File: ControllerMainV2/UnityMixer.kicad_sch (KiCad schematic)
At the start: 50 parts, among them IC17 TMUX6112PWR, IC18 TMUX6112PWR, IC19 TMUX6112PWR, U10 TL072, U18 TL074, U9 TL074

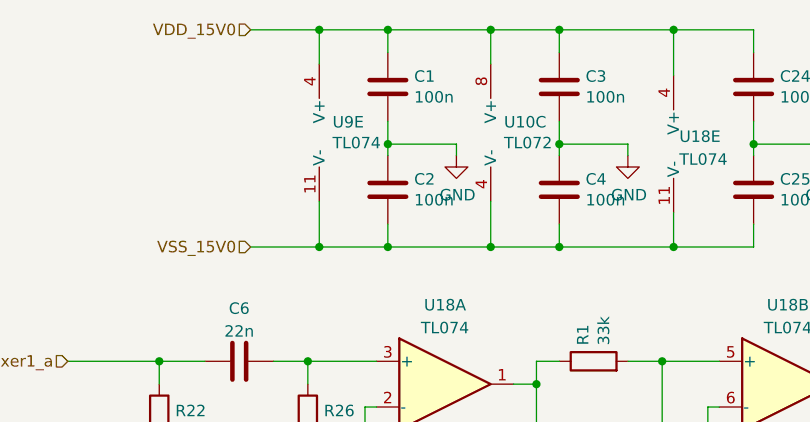
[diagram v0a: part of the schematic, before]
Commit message: Main mostly wired. Push for replacement
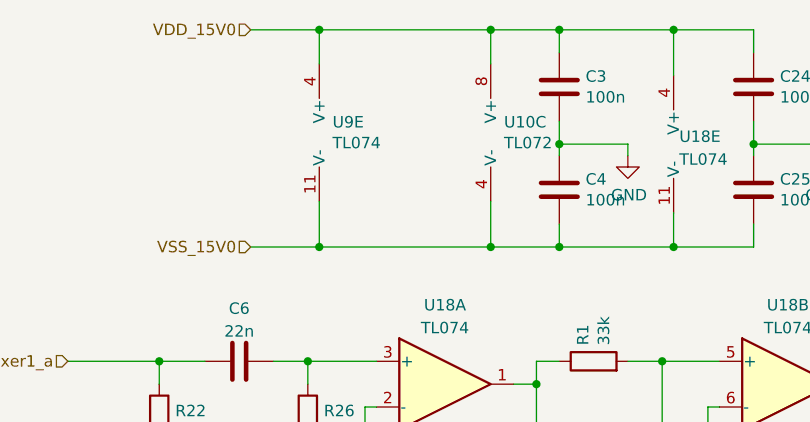
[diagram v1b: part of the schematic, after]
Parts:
- removed C1, C2: 100n, Capacitor_SMD:C_1206_3216Metric_Pad1.33x1.80mm_HandSolder, symbol Device:C
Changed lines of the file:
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@@
   (junction (at 238.125 212.725) (diameter 0) (color 0 0 0 0)
   )
-  (junction (at 100.965 43.815) (diameter 0) (color 0 0 0 0)
-  )
   (junction (at 73.025 220.345) (diameter 0) (color 0 0 0 0)
   )
-  (junction (at 100.965 19.685) (diameter 0) (color 0 0 0 0)
-  )
   (junction (at 131.445 191.135) (diameter 0) (color 0 0 0 0)
   )
@@
   (junction (at 120.015 19.685) (diameter 0) (color 0 0 0 0)
   )
-  (junction (at 100.965 32.385) (diameter 0) (color 0 0 0 0)
-  )
   (junction (at 258.445 78.105) (diameter 0) (color 0 0 0 0)
   )
@@
     (stroke (width 0) (type default) (color 0 0 0 0))
   )
-  (wire (pts (xy 100.965 32.385) (xy 108.585 32.385))
-    (stroke (width 0) (type default) (color 0 0 0 0))
-  )
   (wire (pts (xy 201.295 75.565) (xy 201.295 84.455))
     (stroke (width 0) (type default) (color 0 0 0 0))
@@
     (stroke (width 0) (type default) (color 0 0 0 0))
   )
-  (wire (pts (xy 100.965 43.815) (xy 112.395 43.815))
+  (wire (pts (xy 93.345 43.815) (xy 112.395 43.815))
     (stroke (width 0) (type default) (color 0 0 0 0))
   )
@@
     (stroke (width 0) (type default) (color 0 0 0 0))
   )
-  (wire (pts (xy 100.965 41.275) (xy 100.965 43.815))
-    (stroke (width 0) (type default) (color 0 0 0 0))
-  )
   (wire (pts (xy 255.905 78.105) (xy 258.445 78.105))
     (stroke (width 0) (type default) (color 0 0 0 0))
@@
     (stroke (width 0) (type default) (color 0 0 0 0))
   )
-  (wire (pts (xy 108.585 32.385) (xy 108.585 33.655))
-    (stroke (width 0) (type default) (color 0 0 0 0))
-  )
   (wire (pts (xy 201.295 59.055) (xy 201.295 71.755))
     (stroke (width 0) (type default) (color 0 0 0 0))
   )
-  (wire (pts (xy 100.965 22.225) (xy 100.965 19.685))
-    (stroke (width 0) (type default) (color 0 0 0 0))
-  )
   (wire (pts (xy 238.125 212.725) (xy 239.395 212.725))
     (stroke (width 0) (type default) (color 0 0 0 0))
@@
     (stroke (width 0) (type default) (color 0 0 0 0))
   )
-  (wire (pts (xy 100.965 32.385) (xy 100.965 29.845))
-    (stroke (width 0) (type default) (color 0 0 0 0))
-  )
   (wire (pts (xy 187.325 206.375) (xy 182.245 206.375))
     (stroke (width 0) (type default) (color 0 0 0 0))
   )
-  (wire (pts (xy 100.965 43.815) (xy 93.345 43.815))
-    (stroke (width 0) (type default) (color 0 0 0 0))
-  )
   (wire (pts (xy 128.905 220.345) (xy 133.985 220.345))
     (stroke (width 0) (type default) (color 0 0 0 0))
@@
     (stroke (width 0) (type default) (color 0 0 0 0))
   )
-  (wire (pts (xy 100.965 19.685) (xy 93.345 19.685))
-    (stroke (width 0) (type default) (color 0 0 0 0))
-  )
   (wire (pts (xy 89.535 191.135) (xy 89.535 193.675))
     (stroke (width 0) (type default) (color 0 0 0 0))
@@
     (stroke (width 0) (type default) (color 0 0 0 0))
   )
-  (wire (pts (xy 100.965 19.685) (xy 112.395 19.685))
+  (wire (pts (xy 93.345 19.685) (xy 112.395 19.685))
     (stroke (width 0) (type default) (color 0 0 0 0))
   )
@@
   )
   (wire (pts (xy 97.155 201.295) (xy 116.205 201.295))
-    (stroke (width 0) (type default) (color 0 0 0 0))
-  )
-  (wire (pts (xy 100.965 33.655) (xy 100.965 32.385))
     (stroke (width 0) (type default) (color 0 0 0 0))
   )
@@
       (effects (font (size 1.27 1.27)) hide)
     )
-    (pin "1")
-  )
-  (symbol (lib_id "Device:C") (at 100.965 26.035 0) (unit 1)
-    (in_bom yes) (on_board yes)
-    (property "Reference" "C1" (id 0) (at 103.886 24.8666 0)
-      (effects (font (size 1.27 1.27)) (justify left))
-    )
-    (property "Value" "100n" (id 1) (at 103.886 27.178 0)
-      (effects (font (size 1.27 1.27)) (justify left))
-    )
-    (property "Footprint" "Capacitor_SMD:C_1206_3216Metric_Pad1.33x1.80mm_HandSolder" (id 2) (at 101.9302 29.845 0)
-      (effects (font (size 1.27 1.27)) hide)
-    )
-    (property "Datasheet" "~" (id 3) (at 100.965 26.035 0)
-      (effects (font (size 1.27 1.27)) hide)
-    )
-    (pin "1")
-    (pin "2")
-  )
-  (symbol (lib_id "Device:C") (at 100.965 37.465 0) (unit 1)
-    (in_bom yes) (on_board yes)
-    (property "Reference" "C2" (id 0) (at 103.886 36.2966 0)
-      (effects (font (size 1.27 1.27)) (justify left))
-    )
-    (property "Value" "100n" (id 1) (at 103.886 38.608 0)
-      (effects (font (size 1.27 1.27)) (justify left))
-    )
-    (property "Footprint" "Capacitor_SMD:C_1206_3216Metric_Pad1.33x1.80mm_HandSolder" (id 2) (at 101.9302 41.275 0)
-      (effects (font (size 1.27 1.27)) hide)
-    )
-    (property "Datasheet" "~" (id 3) (at 100.965 37.465 0)
-      (effects (font (size 1.27 1.27)) hide)
-    )
-    (pin "1")
-    (pin "2")
-  )
-  (symbol (lib_id "power:GND") (at 108.585 33.655 0) (unit 1)
-    (in_bom yes) (on_board yes)
-    (property "Reference" "#PWR02" (id 0) (at 108.585 40.005 0)
-      (effects (font (size 1.27 1.27)) hide)
-    )
-    (property "Value" "GND" (id 1) (at 108.712 38.0492 0))
-    (property "Footprint" "" (id 2) (at 108.585 33.655 0)
-      (effects (font (size 1.27 1.27)) hide)
-    )
-    (property "Datasheet" "" (id 3) (at 108.585 33.655 0)
-      (effects (font (size 1.27 1.27)) hide)
-    )

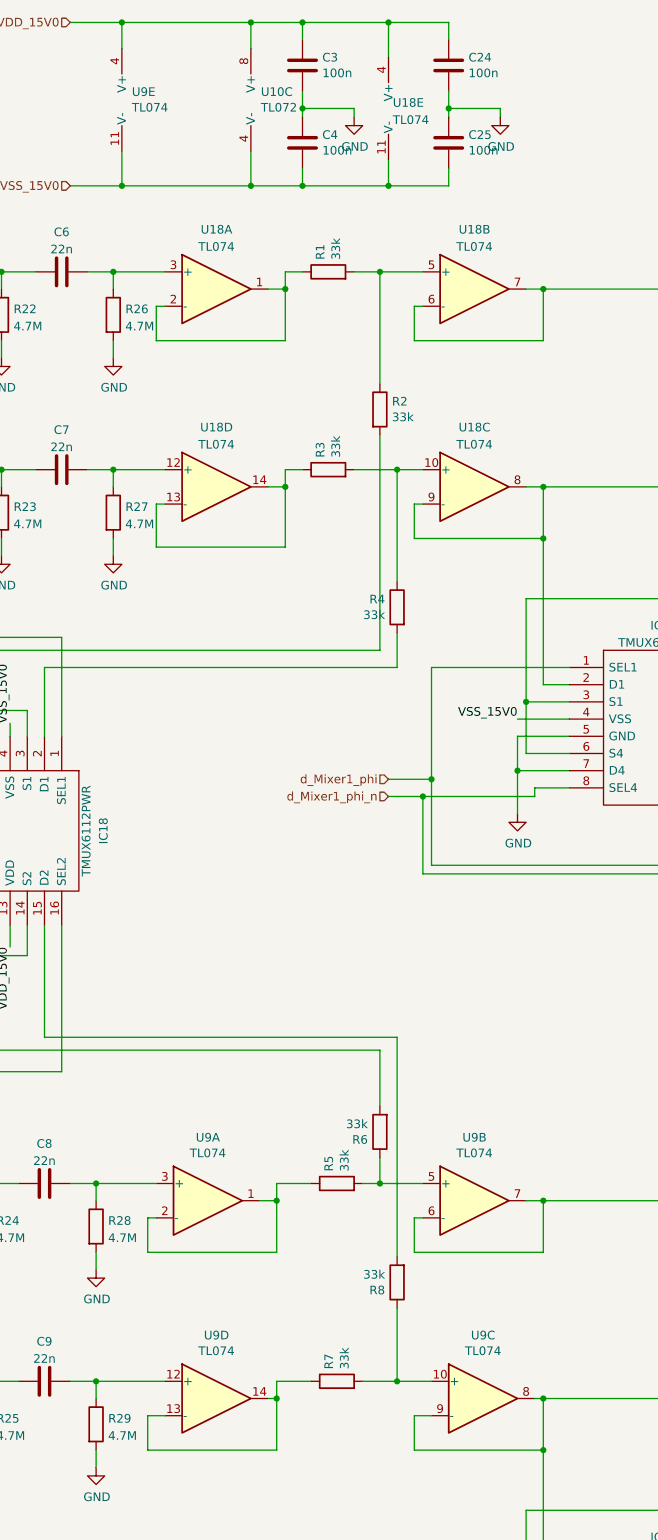
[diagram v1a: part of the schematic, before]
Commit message: Mixer, controll and supply wiring done. Matrix connections missing
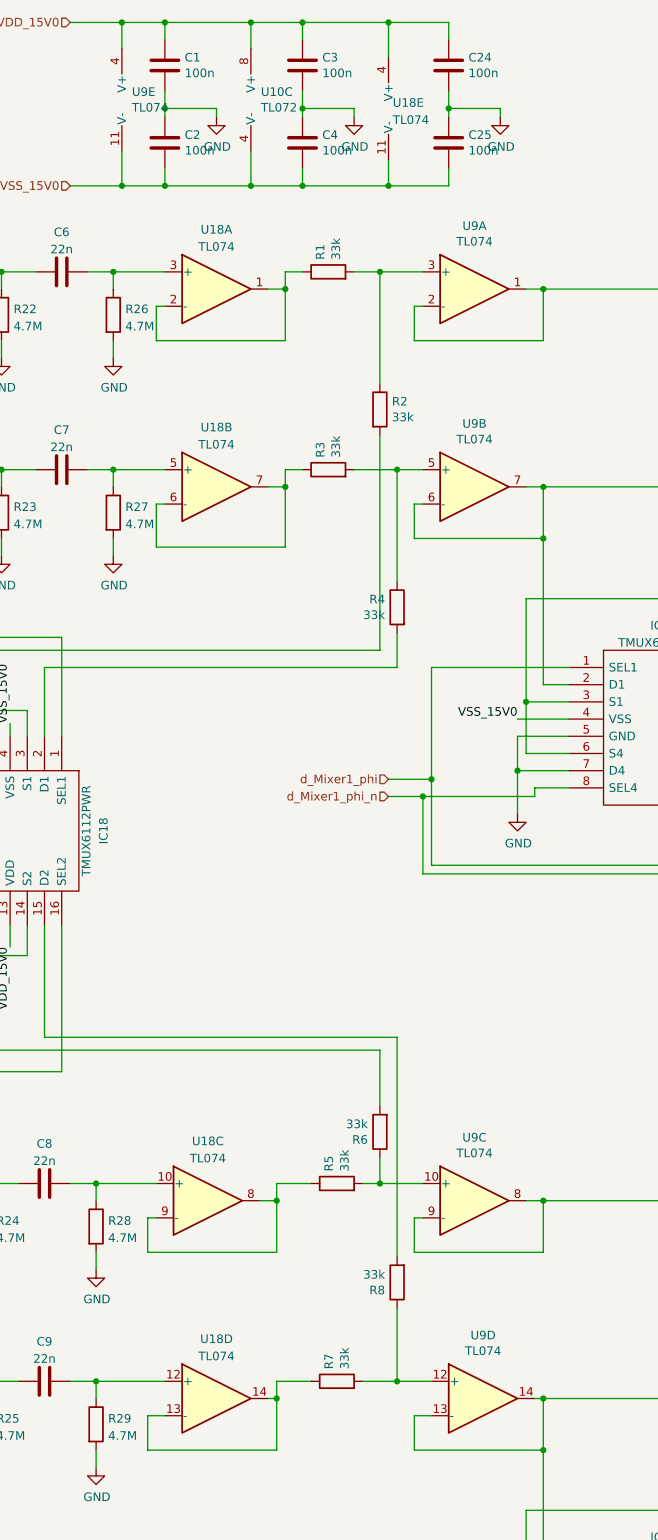
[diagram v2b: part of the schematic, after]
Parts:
- added C1, C2: 100n, Capacitor_SMD:C_1206_3216Metric_Pad1.33x1.80mm_HandSolder, symbol Device:C
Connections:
- net GND: now also C1.2, C2.1
- net VDD_15V0: now also C1.1
- net VSS_15V0: now also C2.2
- net at U9.1, U9.2 (-): now also R9.2; no longer R5.1
- net at C8.2, R28.1: now also U18.10 (+); no longer U9.3 (+)
- net at R5.2, R6.1: now also U9.10 (+); no longer U9.5 (+)
- net at U9.6 (-), U9.7: now also IC17.15 (D2), IC17.2 (D1); no longer R12.1
- net at U18.6 (-), U18.7: now also R3.1; no longer R9.2
- net at R1.2, R2.1: now also U9.3 (+); no longer U18.5 (+)
- net at U18.13 (-), U18.14: now also R7.1; no longer R3.1
- net at R3.2, R4.1: now also U9.5 (+); no longer U18.10 (+)
- net at U9.13 (-), U9.14: now also IC19.15 (D2), IC19.2 (D1); no longer R7.1
- net at R7.2, R8.1: now also U9.12 (+); no longer U9.10 (+)
- net at U9.8, U9.9 (-): now also R12.1; no longer IC19.15 (D2), IC19.2 (D1)
- net at C9.2, R29.1: now also U18.12 (+); no longer U9.12 (+)
- net at U18.8, U18.9 (-): now also R5.1; no longer IC17.15 (D2), IC17.2 (D1)
- net at C7.2, R27.1: now also U18.5 (+); no longer U18.12 (+)
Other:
- moved on the sheet: U18B, U18C, U18D, U9A, U9B, U9C, U9D

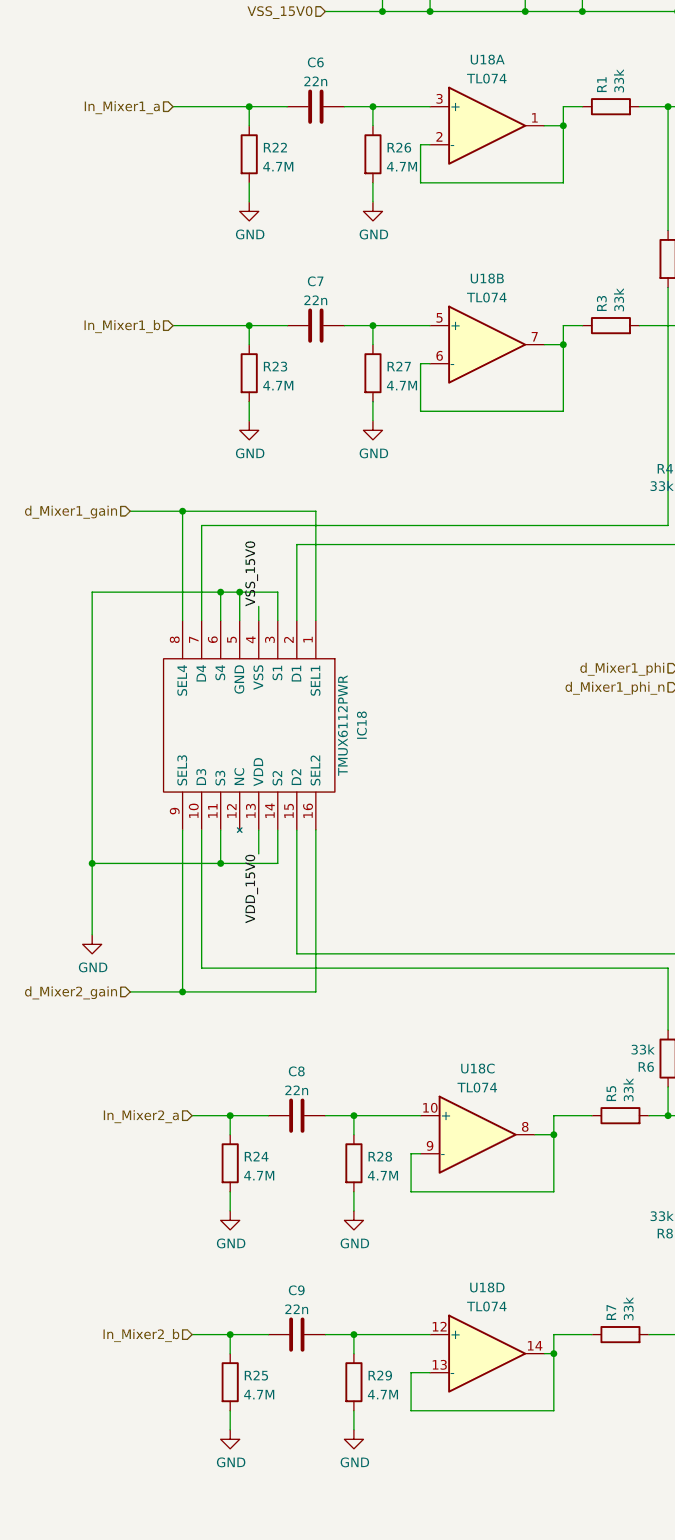
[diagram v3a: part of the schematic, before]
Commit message: Enclosure and faceplate for 8 loops
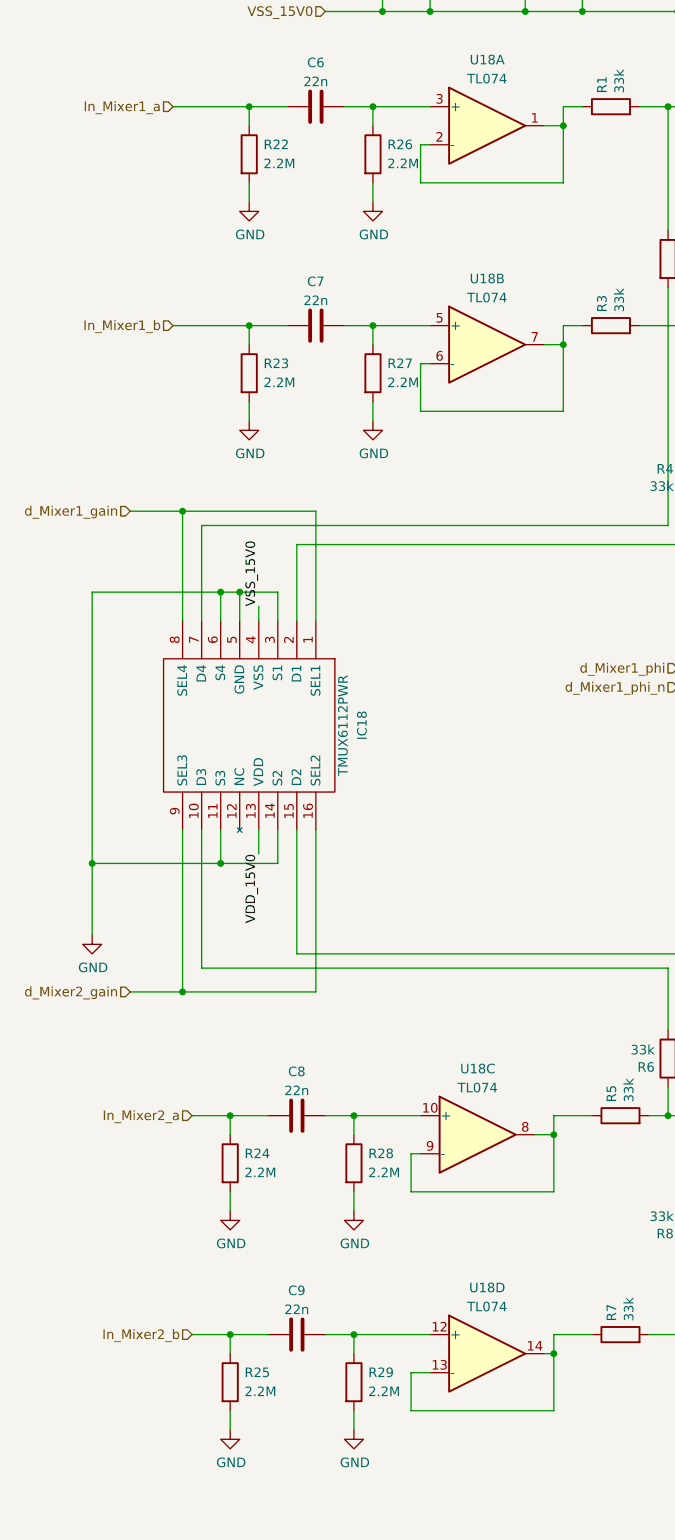
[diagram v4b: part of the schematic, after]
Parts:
- R22, R23, R24, R25, R26, R27, R28, R29: value 4.7M -> 2.2M
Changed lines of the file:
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@@
   (symbol (lib_id "Device:R") (at 73.025 226.695 0) (unit 1)
     (in_bom yes) (on_board yes) (fields_autoplaced)
-    (property "Reference" "R25" (id 0) (at 74.803 225.8603 0)
-      (effects (font (size 1.27 1.27)) (justify left))
-    )
-    (property "Value" "4.7M" (id 1) (at 74.803 228.3972 0)
+    (property "Reference" "R25" (id 0) (at 74.93 225.4249 0)
+      (effects (font (size 1.27 1.27)) (justify left))
+    )
+    (property "Value" "2.2M" (id 1) (at 74.93 227.9649 0)
       (effects (font (size 1.27 1.27)) (justify left))
     )
@@
   (symbol (lib_id "Device:R") (at 75.565 62.865 0) (unit 1)
     (in_bom yes) (on_board yes) (fields_autoplaced)
-    (property "Reference" "R22" (id 0) (at 77.343 62.0303 0)
-      (effects (font (size 1.27 1.27)) (justify left))
-    )
-    (property "Value" "4.7M" (id 1) (at 77.343 64.5672 0)
+    (property "Reference" "R22" (id 0) (at 77.47 61.5949 0)
+      (effects (font (size 1.27 1.27)) (justify left))
+    )
+    (property "Value" "2.2M" (id 1) (at 77.47 64.1349 0)
       (effects (font (size 1.27 1.27)) (justify left))
     )
@@
   (symbol (lib_id "Device:R") (at 89.535 197.485 0) (unit 1)
     (in_bom yes) (on_board yes) (fields_autoplaced)
-    (property "Reference" "R28" (id 0) (at 91.313 196.6503 0)
-      (effects (font (size 1.27 1.27)) (justify left))
-    )
-    (property "Value" "4.7M" (id 1) (at 91.313 199.1872 0)
+    (property "Reference" "R28" (id 0) (at 91.44 196.2149 0)
+      (effects (font (size 1.27 1.27)) (justify left))
+    )
+    (property "Value" "2.2M" (id 1) (at 91.44 198.7549 0)
       (effects (font (size 1.27 1.27)) (justify left))
     )
@@
   (symbol (lib_id "Device:R") (at 73.025 197.485 0) (unit 1)
     (in_bom yes) (on_board yes) (fields_autoplaced)
-    (property "Reference" "R24" (id 0) (at 74.803 196.6503 0)
-      (effects (font (size 1.27 1.27)) (justify left))
-    )
-    (property "Value" "4.7M" (id 1) (at 74.803 199.1872 0)
+    (property "Reference" "R24" (id 0) (at 74.93 196.2149 0)
+      (effects (font (size 1.27 1.27)) (justify left))
+    )
+    (property "Value" "2.2M" (id 1) (at 74.93 198.7549 0)
       (effects (font (size 1.27 1.27)) (justify left))
     )
@@
   (symbol (lib_id "Device:R") (at 89.535 226.695 0) (unit 1)
     (in_bom yes) (on_board yes) (fields_autoplaced)
-    (property "Reference" "R29" (id 0) (at 91.313 225.8603 0)
-      (effects (font (size 1.27 1.27)) (justify left))
-    )
-    (property "Value" "4.7M" (id 1) (at 91.313 228.3972 0)
+    (property "Reference" "R29" (id 0) (at 91.44 225.4249 0)
+      (effects (font (size 1.27 1.27)) (justify left))
+    )
+    (property "Value" "2.2M" (id 1) (at 91.44 227.9649 0)
       (effects (font (size 1.27 1.27)) (justify left))
     )
@@
   (symbol (lib_id "Device:R") (at 92.075 62.865 0) (unit 1)
     (in_bom yes) (on_board yes) (fields_autoplaced)
-    (property "Reference" "R26" (id 0) (at 93.853 62.0303 0)
-      (effects (font (size 1.27 1.27)) (justify left))
-    )
-    (property "Value" "4.7M" (id 1) (at 93.853 64.5672 0)
+    (property "Reference" "R26" (id 0) (at 93.98 61.5949 0)
+      (effects (font (size 1.27 1.27)) (justify left))
+    )
+    (property "Value" "2.2M" (id 1) (at 93.98 64.1349 0)
       (effects (font (size 1.27 1.27)) (justify left))
     )
@@
   (symbol (lib_id "Device:R") (at 92.075 92.075 0) (unit 1)
     (in_bom yes) (on_board yes) (fields_autoplaced)
-    (property "Reference" "R27" (id 0) (at 93.853 91.2403 0)
-      (effects (font (size 1.27 1.27)) (justify left))
-    )
-    (property "Value" "4.7M" (id 1) (at 93.853 93.7772 0)
+    (property "Reference" "R27" (id 0) (at 93.98 90.8049 0)
+      (effects (font (size 1.27 1.27)) (justify left))
+    )
+    (property "Value" "2.2M" (id 1) (at 93.98 93.3449 0)
       (effects (font (size 1.27 1.27)) (justify left))
     )
@@
   (symbol (lib_id "Device:R") (at 75.565 92.075 0) (unit 1)
     (in_bom yes) (on_board yes) (fields_autoplaced)
-    (property "Reference" "R23" (id 0) (at 77.343 91.2403 0)
-      (effects (font (size 1.27 1.27)) (justify left))
-    )
-    (property "Value" "4.7M" (id 1) (at 77.343 93.7772 0)
-      (effects (font (size 1.27 1.27)) (justify left))
-    )
+    (property "Reference" "R23" (id 0) (at 77.47 90.8049 0)
+      (effects (font (size 1.27 1.27)) (justify left))
+    )
+    (property "Value" "2.2M" (id 1) (at 77.47 93.3449 0)
+      (effects (font (size 1.27 1.27)) (justify left))
+    )
